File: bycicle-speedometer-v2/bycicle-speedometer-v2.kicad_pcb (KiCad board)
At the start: 2 copper layers, 2 parts, among them J1 Conn_01x04_Pin

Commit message: initiated schematic update
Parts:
- removed uP1: ProMini2, Pro mini:Pro_Mini
- added U1: ESP-12E, ESP8266:ESP-12E, F.Cu at (87.0, 79.0)

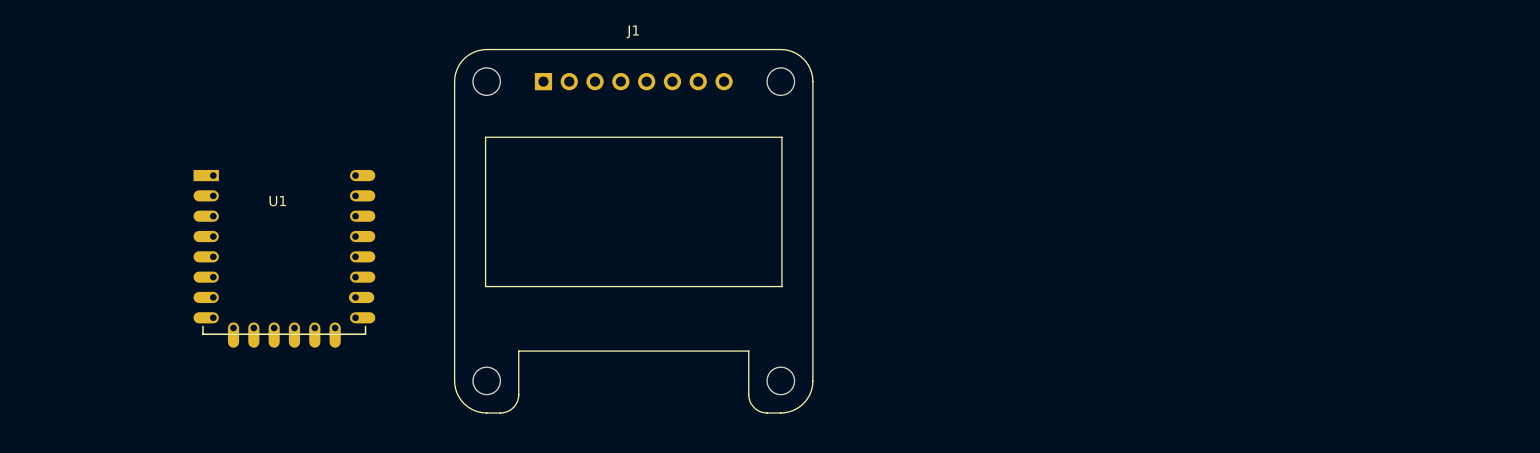
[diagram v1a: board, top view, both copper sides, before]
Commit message: schematic edited a bit
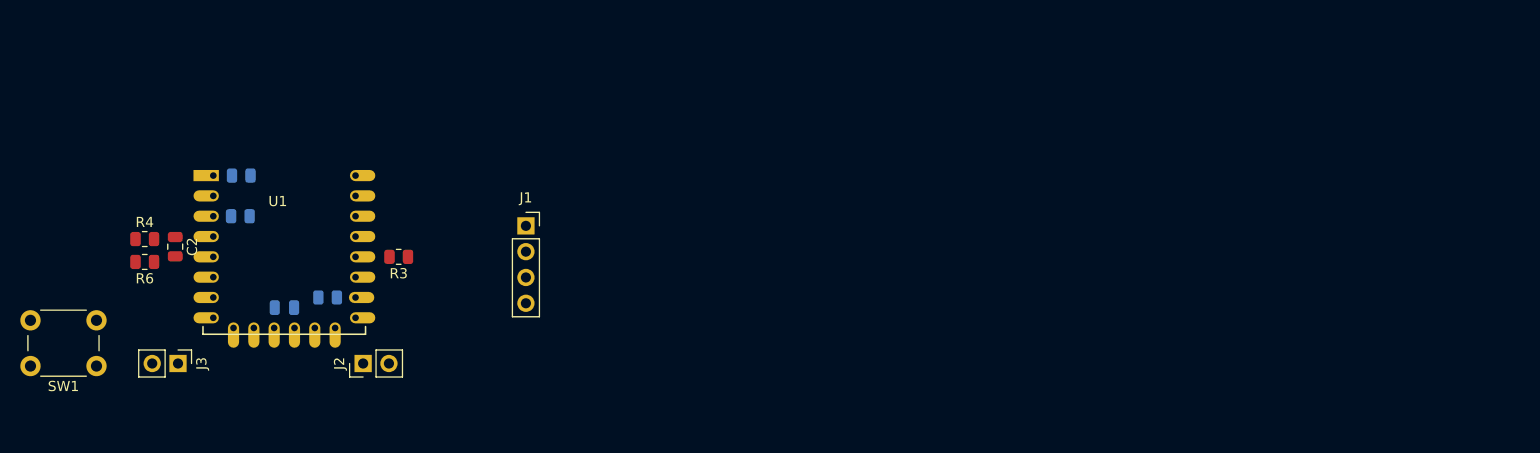
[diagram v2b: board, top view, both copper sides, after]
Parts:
- added C1: 100n, Capacitor_SMD:C_0805_2012Metric, B.Cu at (94.0, 92.0)
- added C2: 1u, Capacitor_SMD:C_0805_2012Metric, F.Cu at (83.2, 86.0)
- added J2: Conn_01x02_Pin, Connector_PinHeader_2.54mm:PinHeader_1x02_P2.54mm_Vertical, F.Cu at (101.8, 97.5)
- added J3: Conn_01x02_Pin, Connector_PinHeader_2.54mm:PinHeader_1x02_P2.54mm_Vertical, F.Cu at (83.5, 97.5)
- added R1: 10k, Resistor_SMD:R_0805_2012Metric, B.Cu at (89.7, 83.0)
- added R2: 10k, Resistor_SMD:R_0805_2012Metric, B.Cu at (89.8, 79.0)
- added R3: 10k, Resistor_SMD:R_0805_2012Metric, F.Cu at (105.2, 87.0)
- added R4: 10k, Resistor_SMD:R_0805_2012Metric, F.Cu at (80.2, 85.2)
- added R5: R, Resistor_SMD:R_0805_2012Metric, B.Cu at (98.2, 91.0)
- added R6: 47k, Resistor_SMD:R_0805_2012Metric, F.Cu at (80.2, 87.5)
- added SW1: SW_Push_Dual, Button_Switch_THT:SW_PUSH_6mm, F.Cu at (75.5, 97.8)
- J1: footprint Display:Adafruit_SSD1306 -> Connector_PinSocket_2.54mm:PinSocket_1x04_P2.54mm_Vertical
- moved J1 14.3 mm to (117.8, 84.0)
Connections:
- J1 pad 1: unconnected-(J1-Pin_1-Pad1) -> SDA
- J1 pad 2: unconnected-(J1-Pin_2-Pad2) -> SCL
- J1 pad 3: unconnected-(J1-Pin_3-Pad3) -> VCC
- J1 pad 4: unconnected-(J1-Pin_4-Pad4) -> GND
- U1 pad 1: unconnected-(U1-REST-Pad1) -> Net-(U1-REST)
- U1 pad 10: unconnected-(U1-GPIO15-Pad10) -> Net-(U1-GPIO15)
- U1 pad 12: unconnected-(U1-GPIO0-Pad12) -> Prog
- U1 pad 13: unconnected-(U1-GPIO4-Pad13) -> SDA
- U1 pad 14: unconnected-(U1-GPIO5-Pad14) -> SCL
- U1 pad 3: unconnected-(U1-CH_PD-Pad3) -> Net-(U1-CH_PD)
- U1 pad 4: unconnected-(U1-GPIO16-Pad4) -> Sensor
- U1 pad 8: unconnected-(U1-VCC-Pad8) -> Net-(U1-VCC)
- U1 pad 9: unconnected-(U1-GND-Pad9) -> GND

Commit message: edited schematic diagram
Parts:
- added C3: 10u, Capacitor_SMD:CP_Elec_5x4.5, F.Cu at (210.8, 71.6)
- added C4: 10u, Capacitor_SMD:CP_Elec_5x4.5, F.Cu at (197.6, 71.6)
- added D1: LED, LED_THT:LED_D5.0mm, F.Cu at (160.0, 92.5)
- added D2: LED, LED_THT:LED_D5.0mm, F.Cu at (169.7, 92.5)
- added D3: LED, LED_THT:LED_D5.0mm, F.Cu at (179.3, 92.5)
- added D4: LED, LED_THT:LED_D5.0mm, F.Cu at (189.0, 92.5)
- added D5: LED, LED_THT:LED_D5.0mm, F.Cu at (198.6, 92.5)
- added D6: LED, LED_THT:LED_D5.0mm, F.Cu at (208.3, 92.5)
- added R7: 10k, Resistor_SMD:R_0805_2012Metric, F.Cu at (173.6, 78.7)
- added R8: 10k, Resistor_SMD:R_0805_2012Metric, F.Cu at (173.6, 81.3)
- added R9: 10k, Resistor_SMD:R_0805_2012Metric, F.Cu at (173.6, 83.8)
- added U2: AMS1117-3.3, Package_TO_SOT_SMD:SOT-223-3_TabPin2, F.Cu at (204.2, 71.6)
- J1: value Conn_01x04_Pin -> Conn_01x02_Pin; footprint Connector_PinSocket_2.54mm:PinSocket_1x04_P2.54mm_Vertical -> TerminalBlock_Phoenix:TerminalBlock_Phoenix_MKDS-1,5-2-5.08_1x02_P5.08mm_Horizontal
- J3: footprint Connector_PinHeader_2.54mm:PinHeader_1x02_P2.54mm_Vertical -> TerminalBlock_Phoenix:TerminalBlock_Phoenix_MKDS-1,5-2-5.08_1x02_P5.08mm_Horizontal
- R3: moved to B.Cu
- moved SW1 100.6 mm to (173.4, 74.9)
- moved J2 96.5 mm to (197.1, 82.6), turned to 180 degrees
- moved R1 91.3 mm to (180.6, 75.2)
- moved C1 91.3 mm to (184.9, 84.2)
- moved R2 91.3 mm to (180.7, 71.2)
- moved R5 91.3 mm to (189.2, 83.2)
- moved U1 91.3 mm to (177.9, 71.1)
- moved J1 90.6 mm to (208.3, 80.3), turned to -90 degrees
- moved R4 89.9 mm to (170.1, 81.3)
- moved R6 89.9 mm to (170.1, 83.8)
- moved C2 87.1 mm to (170.0, 78.7), turned to 0 degrees
- moved R3 84.1 mm to (189.0, 79.2), turned to 0 degrees
- moved J3 80.6 mm to (162.3, 80.3)
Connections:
- J1 pad 1: SDA -> VCC
- J1 pad 2: SCL -> GND
- J3 pad 1: VCC -> 3V3
- R1 pad 1: VCC -> 3V3
- R2 pad 1: VCC -> 3V3
- R3 pad 1: VCC -> 3V3
- U1 pad 13: SDA -> unconnected-(U1-GPIO4-Pad13)
- U1 pad 14: SCL -> unconnected-(U1-GPIO5-Pad14)
- U1 pad 5: unconnected-(U1-GPIO14-Pad5) -> led_a
- U1 pad 6: unconnected-(U1-GPIO12-Pad6) -> led_b
- U1 pad 7: unconnected-(U1-GPIO13-Pad7) -> led_c
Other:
- board outline added: 58 x 30 mm

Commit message: edited schematics
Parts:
- removed C3, C4: 10u, Capacitor_SMD:CP_Elec_5x4.5
- removed U2: AMS1117-3.3, Package_TO_SOT_SMD:SOT-223-3_TabPin2
- added J4: Conn_01x03_Pin, Connector_PinHeader_2.54mm:PinHeader_1x03_P2.54mm_Vertical, F.Cu at (203.2, 72.1)

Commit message: edited schematics
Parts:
- moved J4 3.92 mm to (199.5, 71.0)
- moved C1 2.22 mm to (184.9, 82.0)
- moved R1 2.22 mm to (180.6, 73.0)
- moved R2 2.22 mm to (180.7, 69.0)
- moved R3 2.22 mm to (189.0, 77.0)
- moved R5 2.22 mm to (189.2, 81.0)
- moved U1 2.22 mm to (177.9, 68.9)
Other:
- outline, holes or cut-outs redrawn
- board text added: "+"
- board text added: "-"
- board text added: "1.8-5V to 3V3"
- board text added: "3V3"
- board text added: "<- 3.7V battery here"
- board text added: ">30km/h"
- board text added: ">5km/h"
- board text added: "Bicycle odometer with ESP-12 and reed sensor FritzenLab.net && FritzenLab.com.br"
- board text added: "Reed sensor here ->"
- board text added: "Reset"
- board text added: "VCC"

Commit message: created fabrication files
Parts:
- R5: value R -> 10k
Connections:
- C1 pad 1: Net-(U1-VCC) -> 3V3
- U1 pad 8: Net-(U1-VCC) -> 3V3
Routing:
- net 3V3: track 0.00 -> 75.8 mm, vias 0 -> 2
- net Net-(D1-A): track 0.00 -> 62.0 mm, vias 0 -> 1
- net Net-(D3-K): track 0.00 -> 45.1 mm
- net Net-(D1-K): track 0.00 -> 43.4 mm
- net Sensor: track 0.00 -> 15.9 mm, vias 0 -> 1
- net VCC: track 0.00 -> 10.8 mm
- net Net-(J3-Pin_2): track 0.00 -> 10.1 mm
- net Prog: track 0.00 -> 8.55 mm
- net Net-(U1-REST): track 0.00 -> 7.04 mm
- net led_c: track 0.00 -> 5.02 mm
- net led_b: track 0.00 -> 4.39 mm
- net led_a: track 0.00 -> 4.17 mm
- net Net-(U1-GPIO15): track 0.00 -> 1.88 mm
- net Net-(U1-CH_PD): track 0.00 -> 1.81 mm
- net GND: vias 0 -> 2
- added copper zone on B.Cu, net GND
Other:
- board text added: "FritzenLab.net && FritzenLab.com.br"
- board text added: "Reed switch here ->"
- board text removed: "Reed sensor here ->"
